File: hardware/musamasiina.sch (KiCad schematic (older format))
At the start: 7 parts

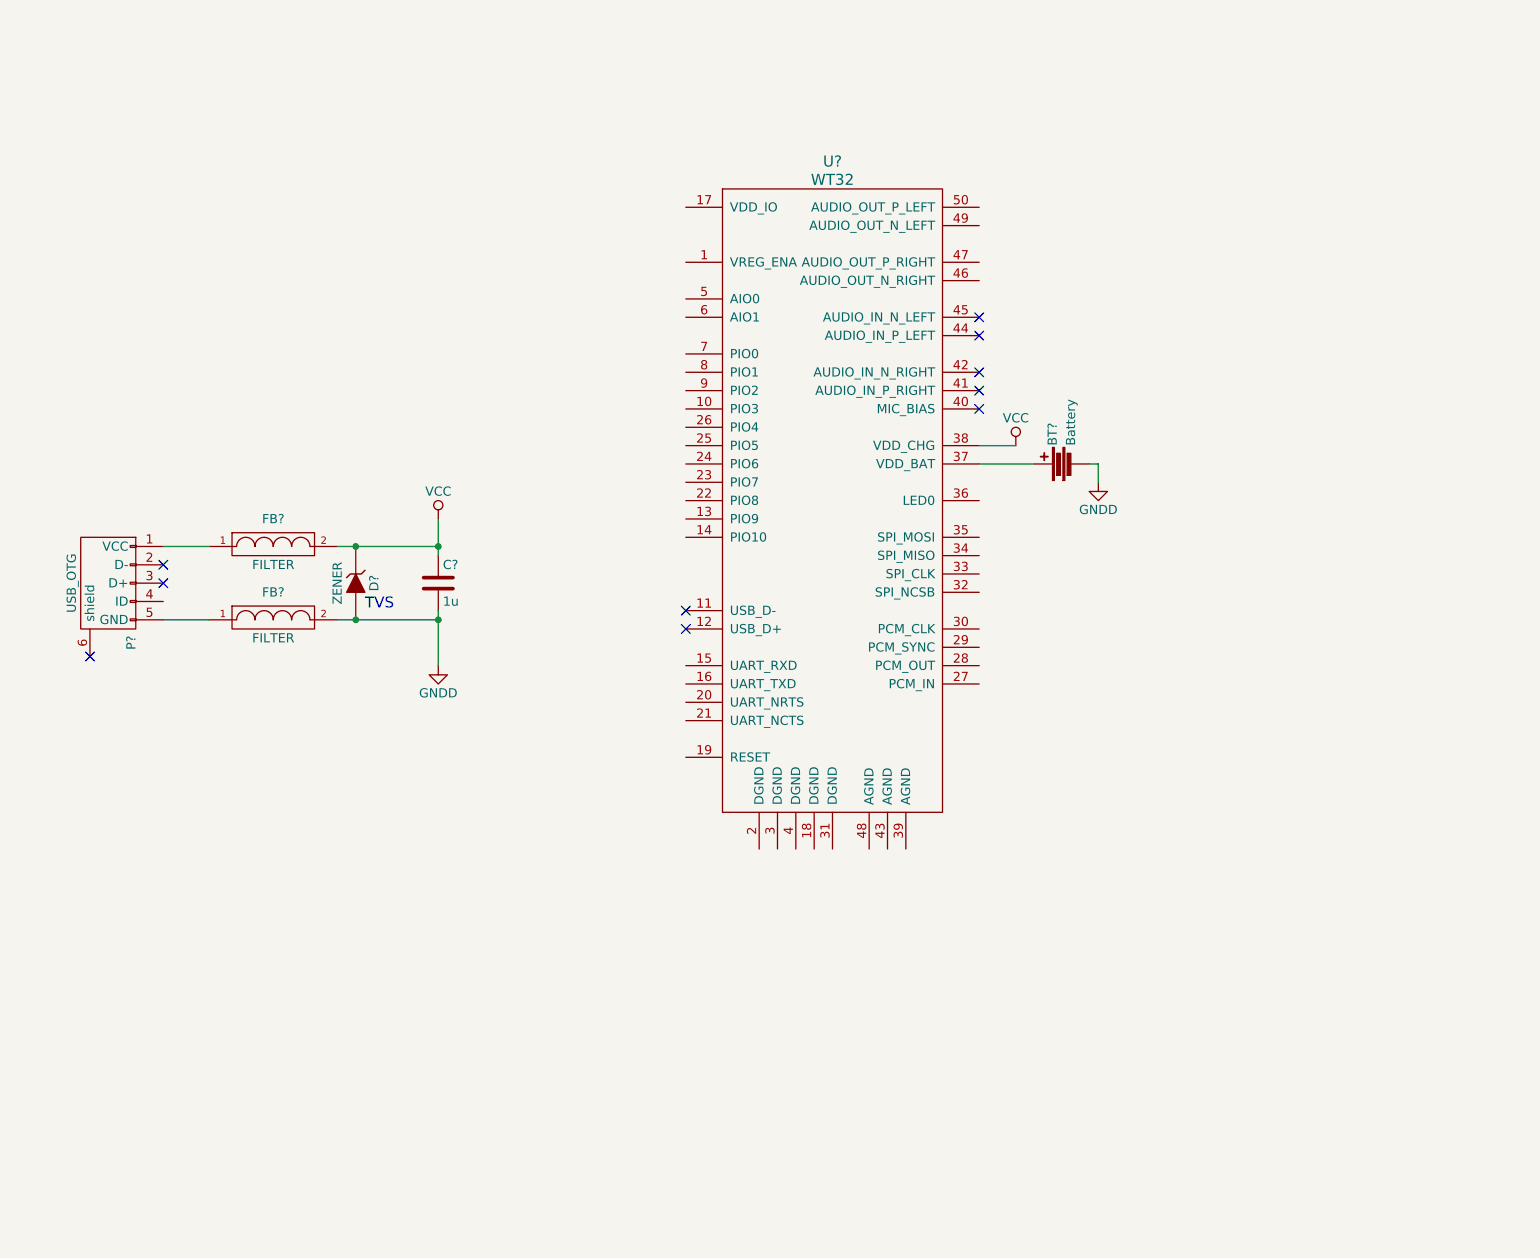
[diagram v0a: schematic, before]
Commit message: Add analog sections to schematic
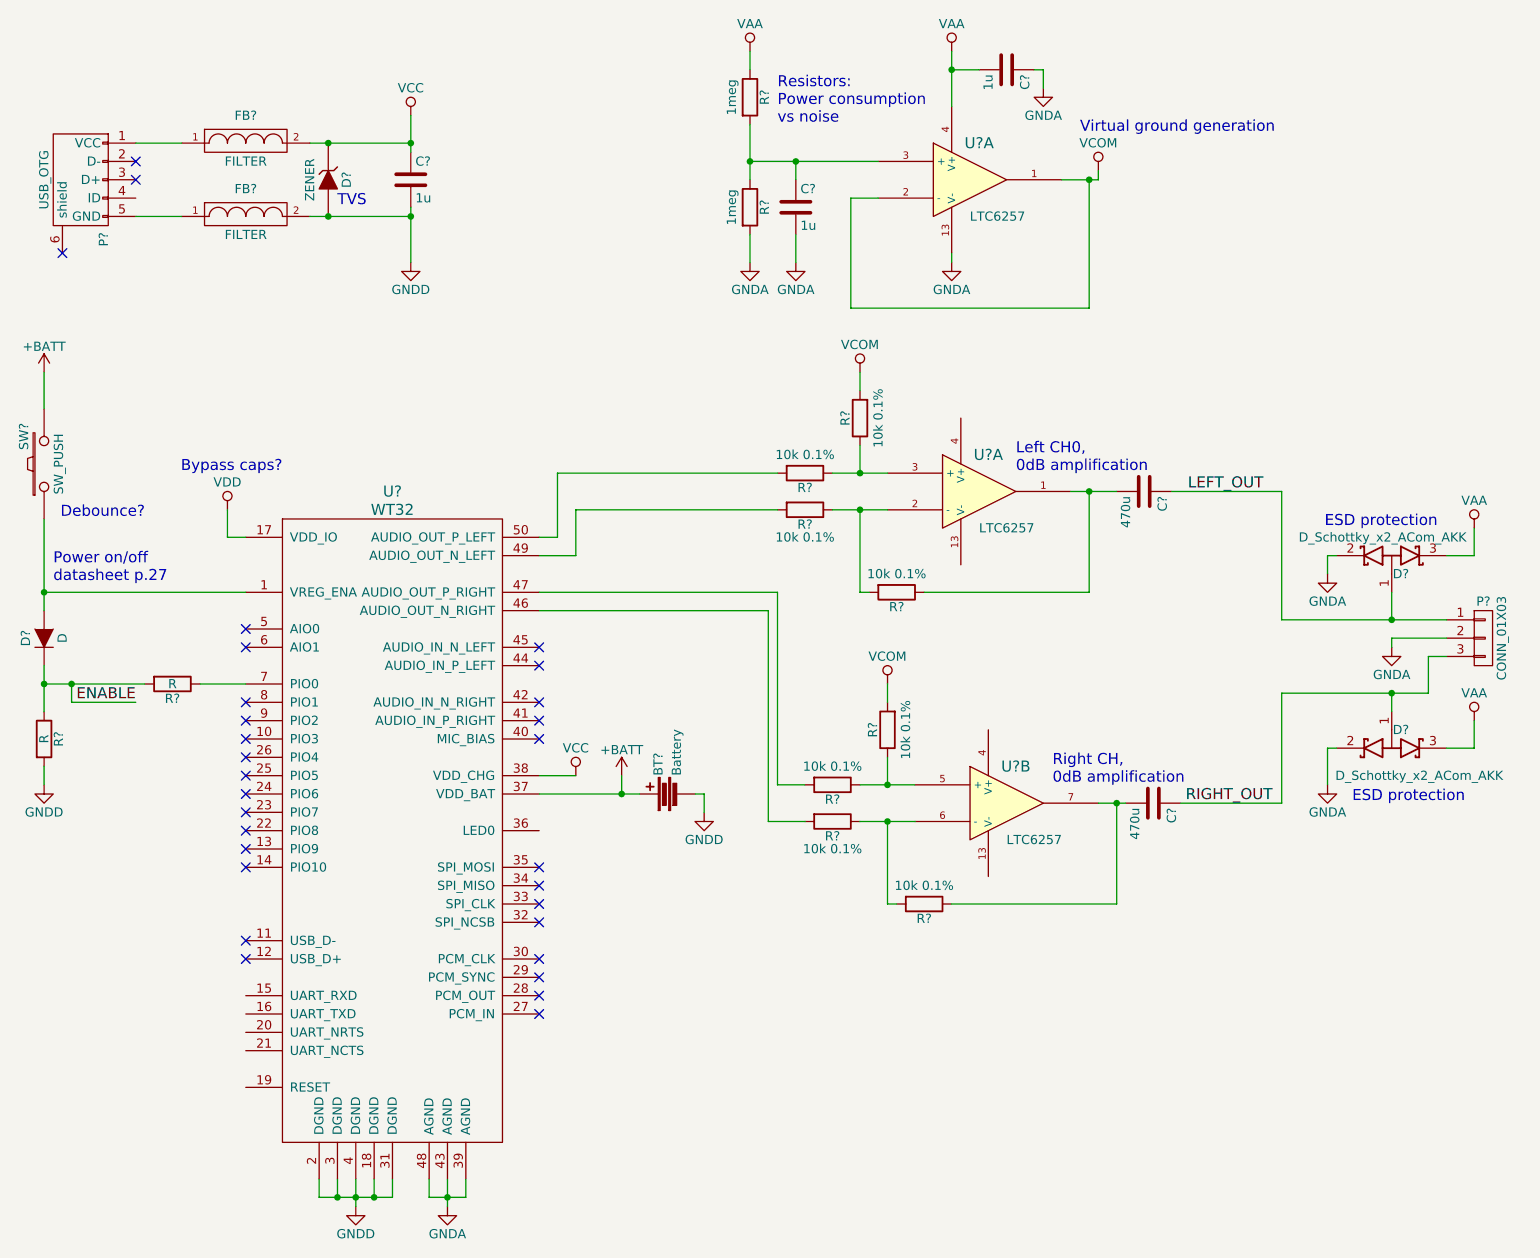
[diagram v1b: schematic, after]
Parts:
- added C? (x2): 1u, symbol C
- added C? (x2): 470u, symbol C
- added D?: D, symbol D
- added D? (x2): D_Schottky_x2_ACom_AKK, symbol D_Schottky_x2_ACom_AKK
- added P?: CONN_01X03, symbol CONN_01X03
- added R? (x8): 10k 0.1%, symbol R
- added R? (x2): 1meg, symbol R
- added R? (x2): R, symbol R
- added SW?: SW_PUSH, symbol SW_PUSH
- added U? (x3): LTC6257, symbol LTC6242
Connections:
- net GNDD: now also U?.18 (DGND), U?.2 (DGND), U?.3 (DGND), U?.31 (DGND), U?.4 (DGND), R?.2
- net at U?.1 (VREG_ENA): now also D?.2 (A), SW?.1
- net VDD: now reaches U?.17 (VDD_IO)
- net +BATT: now reaches BT?.1, U?.37 (VDD_BAT)
- net +BATT: now also SW?.2
- net GNDA: now reaches U?.39 (AGND)
- net GNDA: now also U?.43 (AGND), U?.48 (AGND), C?.1, C?.2, D?.2 (K), D?.2 (K), P?.2 (P2), R?.2, U?.13 (V-)
- net at U?.46 (AUDIO_OUT_N_RIGHT): now also R?.2
- net at U?.47 (AUDIO_OUT_P_RIGHT): now also R?.2
- net at U?.49 (AUDIO_OUT_N_LEFT): now also R?.2
- net at U?.50 (AUDIO_OUT_P_LEFT): now also R?.2
- net at U?.7 (PIO0): now also R?.1
- new net: C?.2, R?.1, U?.1
- new net: R?.1, R?.2, U?.2 (-)
- new net: R?.1, R?.1, U?.3 (+)
- new net: C?.1, R?.1, R?.2, U?.3 (+)
- new net: R?.1, R?.1, U?.5 (+)
- new net: R?.1, R?.2, U?.6 (-)
- new net: C?.2, R?.1, U?.7
- new net ENABLE: D?.1 (K), R?.1, R?.2
- new net LEFT_OUT: C?.1, D?.1 (A), P?.1 (P1)
- new net RIGHT_OUT: C?.1, D?.1 (A), P?.3 (P3)
- new net VAA: C?.2, D?.3 (K), D?.3 (K), R?.1, U?.4 (V+)
- new net VCOM: R?.2, R?.2, U?.1, U?.2 (-)
- no-connect marks 10 -> 30
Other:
- note added: "Bypass caps?"
- note added: "Debounce?"
- note added: "ESD protection"
- note added: "Left CH0,\n0dB amplification"
- note added: "Power on/off\ndatasheet p.27"
- note added: "Resistors:\nPower consumption\nvs noise"
- note added: "Right CH,\n0dB amplification"
- note added: "Virtual ground generation"
- moved on the sheet: BT?, C?, D?, FB?, P?, U?

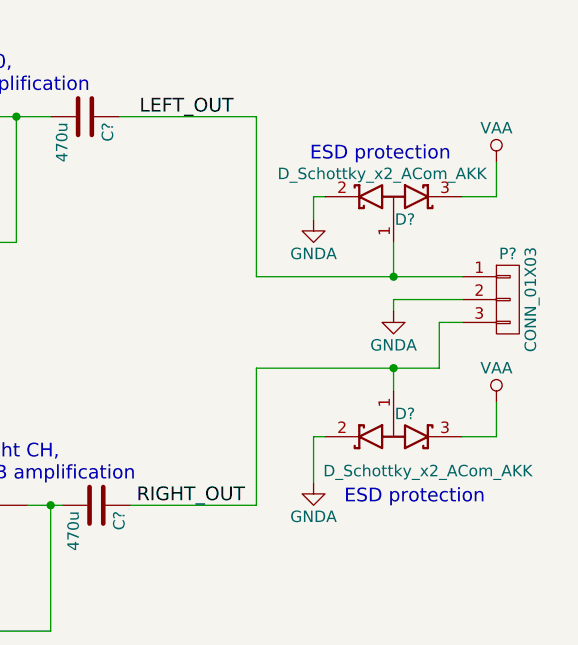
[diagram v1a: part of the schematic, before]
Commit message: Fix ESD-protection diodes
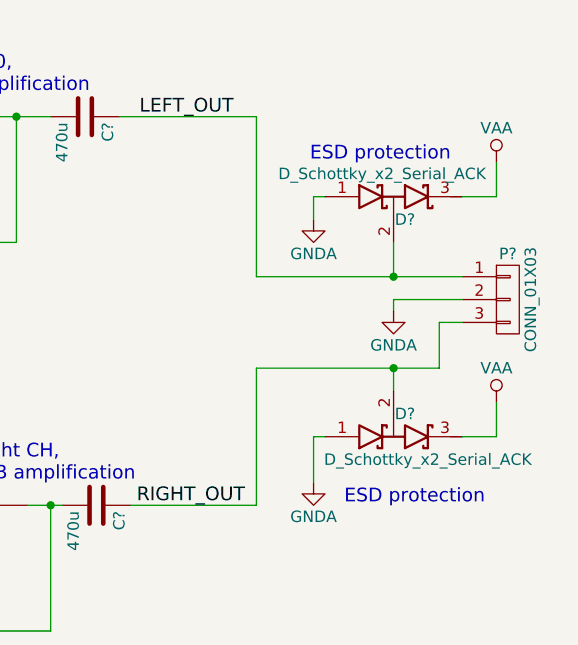
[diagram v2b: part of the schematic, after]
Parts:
- removed D? (x2): D_Schottky_x2_ACom_AKK, symbol D_Schottky_x2_ACom_AKK
- added D? (x2): D_Schottky_x2_Serial_ACK, symbol D_Schottky_x2_Serial_ACK
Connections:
- net GNDA: now also D?.1 (A), D?.1 (A)
- net LEFT_OUT: now also D?.2 (common)
- net RIGHT_OUT: now also D?.2 (common)
- net VAA: now also D?.3 (K), D?.3 (K)
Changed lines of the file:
@@
 Title "poppimASiina"
 Date "2016-05-15"
-Rev "8a44609"
+Rev "4cb9da6"
 Comp "Aivan Sama / Säätökerho"
 Comment1 "http://tinyurl.com/saatomieliset"
@@
 $EndComp
 $Comp
-L D_Schottky_x2_ACom_AKK D?
-U 1 1 573903F5
-P 8200 3600
-F 0 "D?" H 8250 3500 50  0000 C CNN
-F 1 "D_Schottky_x2_ACom_AKK" H 8150 3700 50  0000 C CNN
-F 2 "" H 8200 3600 50  0000 C CNN
-F 3 "" H 8200 3600 50  0000 C CNN
-	1    8200 3600
-	1    0    0    -1
-$EndComp
-$Comp
-L D_Schottky_x2_ACom_AKK D?
-U 1 1 57390538
-P 8200 4650
-F 0 "D?" H 8250 4550 50  0000 C CNN
-F 1 "D_Schottky_x2_ACom_AKK" H 8350 4800 50  0000 C CNN
-F 2 "" H 8200 4650 50  0000 C CNN
-F 3 "" H 8200 4650 50  0000 C CNN
-	1    8200 4650
-	1    0    0    1
-$EndComp
-$Comp
 L CONN_01X03 P?
 U 1 1 5739093E
@@
 Text Notes 8600 4950 2    60   ~ 0
 ESD protection
+$Comp
+L D_Schottky_x2_Serial_ACK D?
+U 1 1 57392FFB
+P 8200 3600
+F 0 "D?" H 8250 3500 50  0000 C CNN
+F 1 "D_Schottky_x2_Serial_ACK" H 8150 3700 50  0000 C CNN
+F 2 "" H 8200 3600 50  0000 C CNN
+F 3 "" H 8200 3600 50  0000 C CNN
+	1    8200 3600
+	1    0    0    -1
+$EndComp
+$Comp
+L D_Schottky_x2_Serial_ACK D?
+U 1 1 57393248
+P 8200 4650
+F 0 "D?" H 8250 4550 50  0000 C CNN
+F 1 "D_Schottky_x2_Serial_ACK" H 8350 4750 50  0000 C CNN
+F 2 "" H 8200 4650 50  0000 C CNN
+F 3 "" H 8200 4650 50  0000 C CNN
+	1    8200 4650
+	1    0    0    1
+$EndComp
 $EndSCHEMATC
